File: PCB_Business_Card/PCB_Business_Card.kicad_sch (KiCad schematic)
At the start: 0 parts

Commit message: Added USB and power circuitry, updated TP4056 -> TP4057
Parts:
- added BT1: Battery_Cell, user_footprints:BatteryHolder_Custom, symbol Device:Battery_Cell
- added C1, C24, C5: 1u, user_footprints:C_0402_1005Metric_small_pads, symbol Device:C
- added C23: 100n, user_footprints:C_0402_1005Metric_small_pads, symbol Device:C
- added D1: Schottky Diode, Diode_SMD:D_SOD-323, symbol Device:D
- added J1: USB_C_Receptacle_USB2.0_14P, user_footprints:USB_C_PADDLE, symbol Connector:USB_C_Receptacle_USB2.0_14P
- added J3: TP4057, Package_TO_SOT_SMD:SOT-23-6, symbol User_Symbols:TP4057
- added Q6, Q7: HL-2302V, Package_TO_SOT_SMD:SOT-23, symbol User_Symbols:HL-2302V
- added R10: 100, Resistor_SMD:R_0402_1005Metric, symbol Device:R
- added R11, R12: 5K1, Resistor_SMD:R_0402_1005Metric, symbol Device:R
- added R31: 1K, Resistor_SMD:R_0402_1005Metric, symbol Device:R
- added R9: 20K, Resistor_SMD:R_0402_1005Metric, symbol Device:R
- added U2: REG_3.3V, Package_TO_SOT_SMD:SOT-23, symbol Regulator_Linear:NCP1117-3.3_SOT223
- added U5: DW01A, Package_TO_SOT_SMD:SOT-23-6, symbol Battery_Management:DW01A
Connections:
- new net: R31.2, U5.2 (CS)
- new net: BT1.1 (+), C24.1, D1.2 (A), J3.3 (BAT), R10.1
- new net: J1.A5 (CC1), R11.1
- new net: J3.6 (PROG), R9.1
- new net: Q6.1 (G), U5.3 (OC)
- new net: Q6.3 (D), Q7.3 (D)
- new net: J1.B5 (CC2), R12.1
- new net: C23.1, R10.2, U5.5 (VCC)
- new net: BT1.2 (-), C23.2, Q7.2 (S), U5.6 (GND)
- new net: Q7.1 (G), U5.1 (OD)
- new net +3V3: C5.1, U2.2 (VO)
- new net GND: C1.2, C24.2, C5.2, J1.A1 (GND), J1.A12 (GND), J1.B1 (GND), J1.B12 (GND), J1.S1 (SHIELD), J3.2 (GND), J3.5 (STDBY), Q6.2 (S), R11.2, R12.2, R31.1, R9.2, U2.1 (GND)
- new net USB_D+: J1.A6 (D+), J1.B6 (D+)
- new net USB_D-: J1.A7 (D-), J1.B7 (D-)
- new net VBUS: C1.1, D1.1 (K), J1.A4 (VBUS), J1.A9 (VBUS), J1.B4 (VBUS), J1.B9 (VBUS), J3.4 (VCC), U2.3 (VI)
- no-connect marks 0 -> 1
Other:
- note added: "Power"

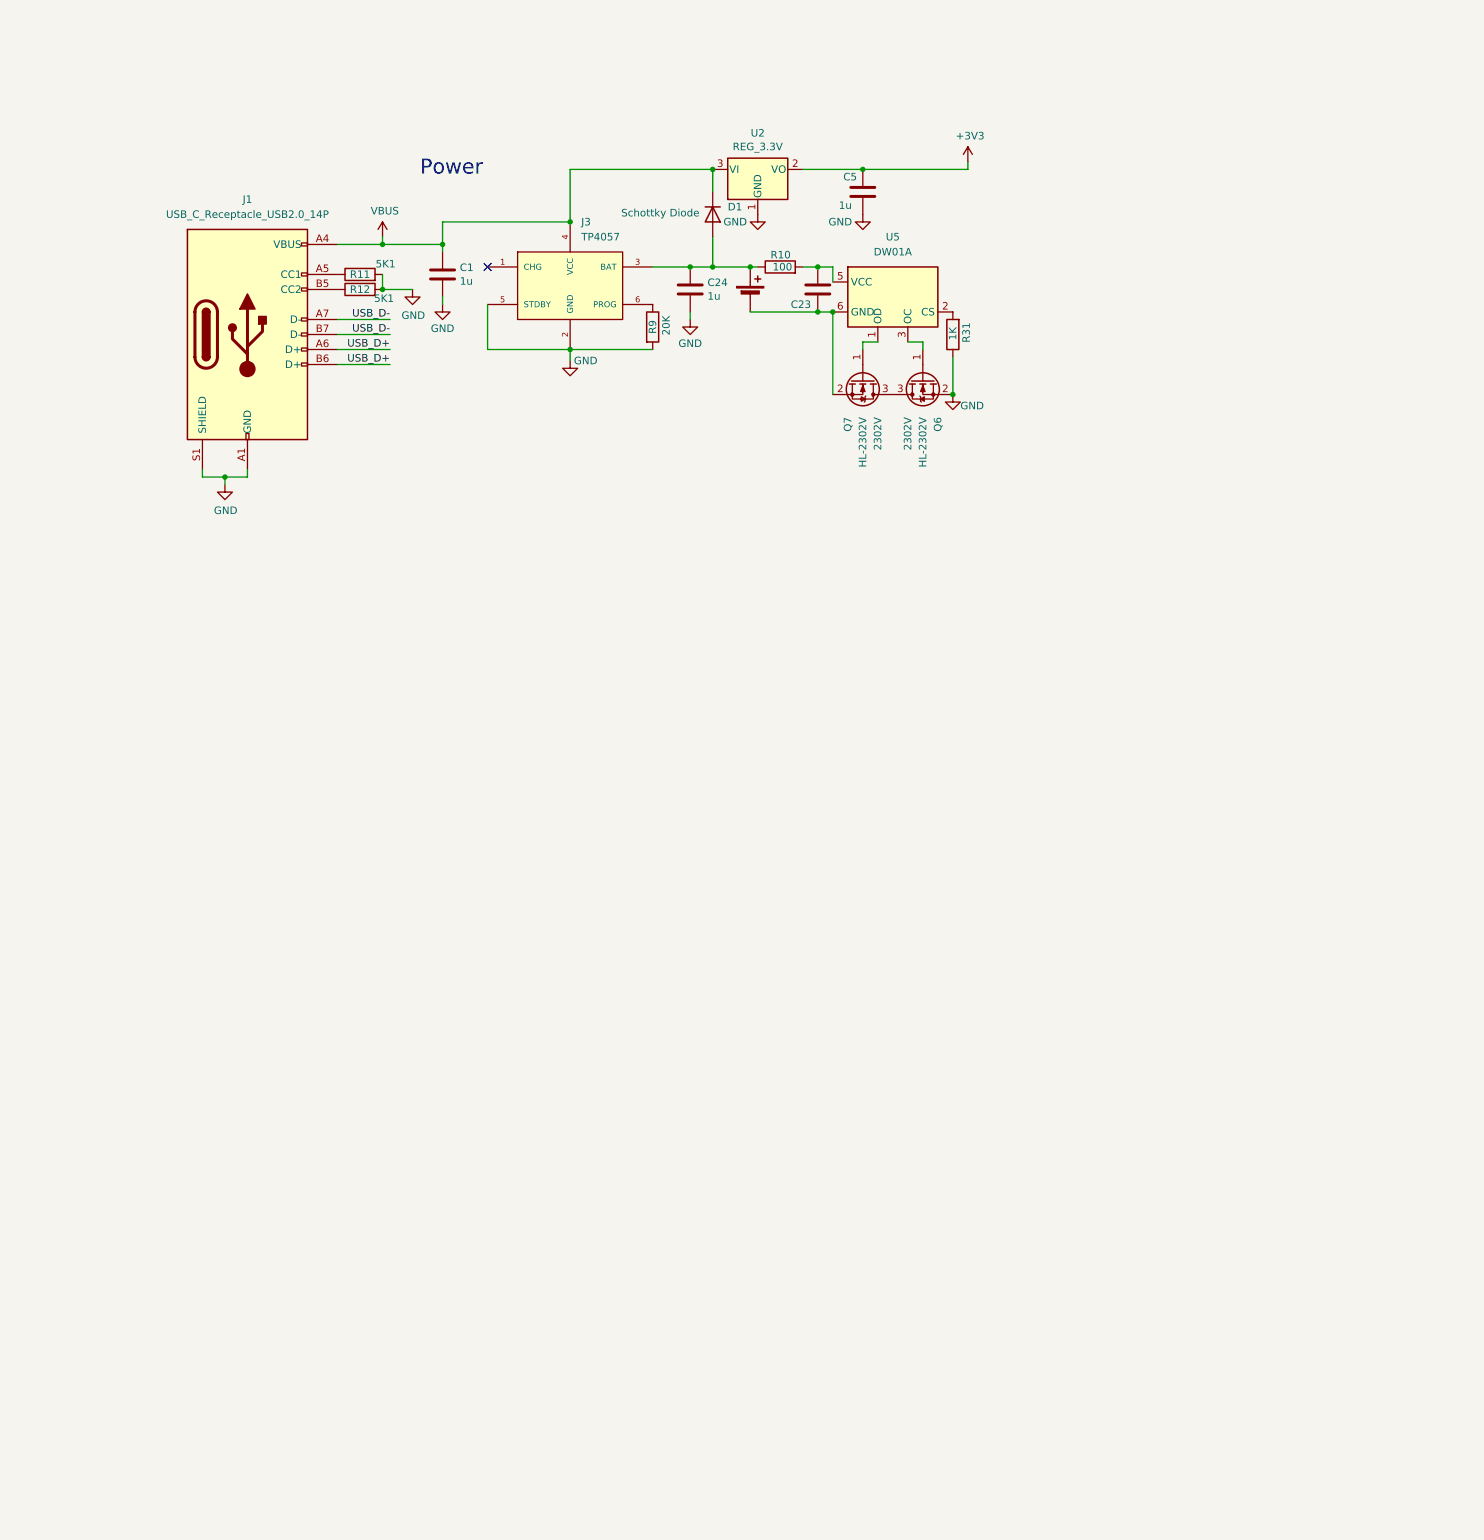
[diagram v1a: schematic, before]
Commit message: feature progress : ok so i added the decoupling capacitors and the flash memory to the circuit a small part is remaining to complete the mcu section
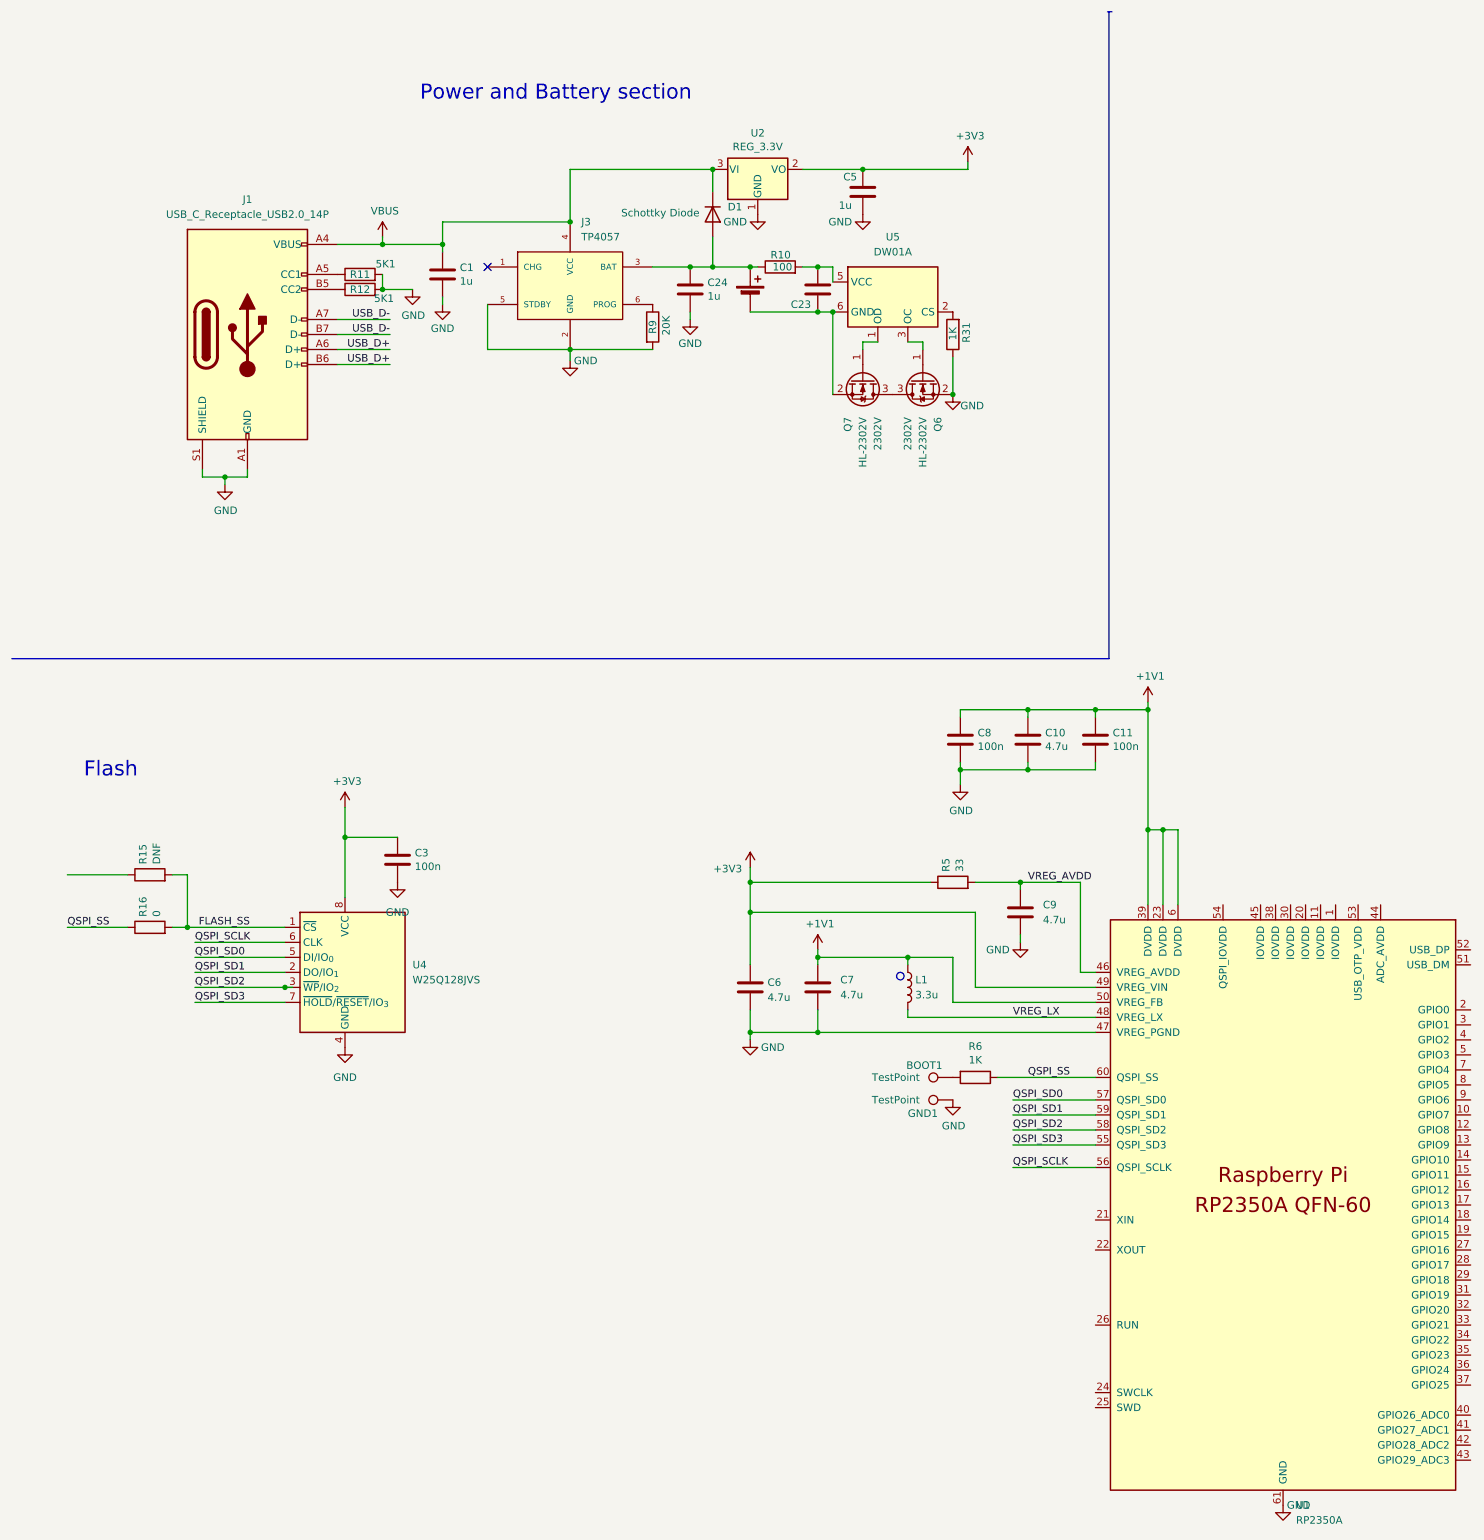
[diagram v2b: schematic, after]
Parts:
- added BOOT1, GND1: TestPoint, TestPoint:TestPoint_Pad_1.0x1.0mm, symbol Connector:TestPoint
- added C10, C6, C7, C9: 4.7u, user_footprints:C_0402_1005Metric_small_pads, symbol Device:C
- added C11, C8: 100n, user_footprints:C_0402_1005Metric_small_pads, symbol Device:C
- added C3: 100n, Capacitor_SMD:C_0402_1005Metric, symbol Device:C
- added L1: 3.3u, RP2350_60QFN_minimal:L_pol_2016, symbol Device:L
- added R15: DNF, Resistor_SMD:R_0402_1005Metric, symbol Device:R
- added R16: 0, Resistor_SMD:R_0402_1005Metric, symbol Device:R
- added R5: 33, Resistor_SMD:R_0402_1005Metric, symbol Device:R
- added R6: 1K, Resistor_SMD:R_0402_1005Metric, symbol Device:R
- added U1: RP2350A, RP2350_60QFN_minimal:RP2350-QFN-60-1EP_7x7_P0.4mm_EP3.4x3.4mm_ThermalVias, symbol MCU_RaspberryPi_RP2350:RP2350_60QFN
- added U4: W25Q128JVS, Package_SO:SOIC-8_5.3x5.3mm_P1.27mm, symbol Memory_Flash:W25Q128JVS
- R11: footprint Resistor_SMD:R_0402_1005Metric -> user_footprints:C_0402_1005Metric_small_pads
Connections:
- net +3V3: now also C3.1, C6.1, R5.1, U1.49 (VREG_VIN), U4.8 (VCC)
- net GND: now also C10.2, C11.2, C3.2, C6.2, C7.2, C8.2, C9.2, GND1.1, U1.47 (VREG_PGND), U1.61 (GND), U4.4 (GND)
- new net: BOOT1.1, R6.2
- new net +1V1: C10.1, C11.1, C7.1, C8.1, L1.1, U1.23 (DVDD), U1.39 (DVDD), U1.50 (VREG_FB), U1.6 (DVDD)
- new net FLASH_SS: R15.2, R16.2, U4.1 (~{CS})
- new net QSPI_SCLK: U1.56 (QSPI_SCLK), U4.6 (CLK)
- new net QSPI_SD0: U1.57 (QSPI_SD0), U4.5 (DI/IO_{0})
- new net QSPI_SD1: U1.59 (QSPI_SD1), U4.2 (DO/IO_{1})
- new net QSPI_SD2: U1.58 (QSPI_SD2), U4.3 (~{WP}/IO_{2})
- new net QSPI_SD3: U1.55 (QSPI_SD3), U4.7 (~{HOLD}/~{RESET}/IO_{3})
- new net QSPI_SS: R16.1, R6.1, U1.60 (QSPI_SS)
- new net VREG_AVDD: C9.1, R5.2, U1.46 (VREG_AVDD)
- new net VREG_LX: L1.2, U1.48 (VREG_LX)
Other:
- note added: "Flash"
- note added: "Power and Battery section"
- note removed: "Power"
- title: (none) -> PCB_Business_Card

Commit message: update: added the neccesary caps and resistors for the flash memory and the flash memory part is completed
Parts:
- added R1: DNF, Resistor_SMD:R_0402_1005Metric, symbol Device:R
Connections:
- net +3V3: now also R1.1
- net FLASH_SS: now also R1.2
- net GPIO0: now reaches R15.1
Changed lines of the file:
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@@
 	)
 	(junction
+		(at 55.88 166.37)
+		(diameter 0)
+		(color 0 0 0 0)
+	)
+	(junction
 		(at 148.59 171.45)
 		(diameter 0)
@@
 	(wire
 		(pts
+			(xy 43.18 171.45) (xy 58.42 171.45)
+		)
+		(stroke
+			(width 0)
+			(type default)
+		)
+	)
+	(wire
+		(pts
 			(xy 67.31 68.58) (xy 76.2 68.58)
 		)
@@
 	(wire
 		(pts
+			(xy 55.88 152.4) (xy 55.88 151.13)
+		)
+		(stroke
+			(width 0)
+			(type default)
+		)
+	)
+	(wire
+		(pts
 			(xy 195.58 129.54) (xy 204.47 129.54)
 		)
@@
 	(wire
 		(pts
-			(xy 58.42 171.45) (xy 43.18 171.45)
+			(xy 173.99 38.1) (xy 173.99 36.83)
 		)
 		(stroke
@@
 	(wire
 		(pts
-			(xy 173.99 38.1) (xy 173.99 36.83)
+			(xy 67.31 71.12) (xy 76.2 71.12)
 		)
 		(stroke
@@
 	(wire
 		(pts
-			(xy 67.31 71.12) (xy 76.2 71.12)
+			(xy 106.68 70.485) (xy 106.68 68.58)
 		)
 		(stroke
@@
 	(wire
 		(pts
-			(xy 106.68 70.485) (xy 106.68 68.58)
+			(xy 106.68 46.99) (xy 106.68 38.1)
 		)
 		(stroke
@@
 	(wire
 		(pts
-			(xy 106.68 46.99) (xy 106.68 38.1)
+			(xy 148.59 180.34) (xy 148.59 184.15)
 		)
 		(stroke
@@
 	(wire
 		(pts
-			(xy 148.59 180.34) (xy 148.59 184.15)
+			(xy 55.88 166.37) (xy 58.42 166.37)
 		)
 		(stroke
@@
 	(wire
 		(pts
+			(xy 55.88 160.02) (xy 55.88 166.37)
+		)
+		(stroke
+			(width 0)
+			(type default)
+		)
+	)
+	(wire
+		(pts
 			(xy 85.09 46.99) (xy 85.09 50.8)
 		)
@@
 	(wire
 		(pts
-			(xy 41.91 166.37) (xy 58.42 166.37)
+			(xy 41.91 166.37) (xy 55.88 166.37)
 		)
 		(stroke
@@
 	(wire
 		(pts
+			(xy 55.88 151.13) (xy 68.58 151.13)
+		)
+		(stroke
+			(width 0)
+			(type default)
+		)
+	)
+	(wire
+		(pts
 			(xy 137.16 163.83) (xy 175.26 163.83)
 		)
@@
 		)
 	)
+	(label "GPIO0"
+		(at 21.59 157.48 0)
+		(effects
+			(font
+				(size 1.27 1.27)
+			)
+			(justify left bottom)
+		)
+	)
 	(label "QSPI_SD1"
 		(at 43.18 173.99 0)
@@
 					(unit 1)
 				)
+			)
+		)
+	)
+	(symbol
+		(lib_id "Device:R")
+		(at 55.88 156.21 0)
+		(unit 1)
+		(body_style 1)
+		(exclude_from_sim no)
+		(in_bom yes)
+		(on_board yes)
+		(in_pos_files yes)
+		(dnp no)
+		(property "Reference" "R1"
+			(at 57.658 155.0416 0)
+			(show_name no)
+			(do_not_autoplace no)
+			(effects
+				(font
+					(size 1.27 1.27)
+				)
+				(justify left)
+			)
+		)
+		(property "Value" "DNF"
+			(at 57.658 157.353 0)
+			(show_name no)
+			(do_not_autoplace no)
+			(effects
+				(font
+					(size 1.27 1.27)
+				)
+				(justify left)
+			)
+		)
+		(property "Footprint" "Resistor_SMD:R_0402_1005Metric"
+			(at 54.102 156.21 90)
+			(hide yes)
+			(show_name no)
+			(do_not_autoplace no)
+			(effects
+				(font
+					(size 1.27 1.27)
+				)
+			)
+		)
+		(property "Datasheet" ""
+			(at 55.88 156.21 0)
+			(hide yes)
+			(show_name no)
+			(do_not_autoplace no)
+			(effects
+				(font
+					(size 1.27 1.27)
+				)
+			)
+		)
+		(property "Description" ""
+			(at 55.88 156.21 0)
+			(show_name no)
+			(do_not_autoplace no)
+			(effects
+				(font
+					(size 1.27 1.27)
+				)
+			)
+		)
+		(pin "1"
+		)
+		(pin "2"
+		)
+		(instances
+			(project "PCB_Business_Card"
+				(path "/72b6ae51-acd1-488c-a7bc-8dc9cbbbee14"
+					(reference "R1")
+					(unit 1)
+				)
